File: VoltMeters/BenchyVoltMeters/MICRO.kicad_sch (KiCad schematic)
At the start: 18 parts, among them Y1 8MHz

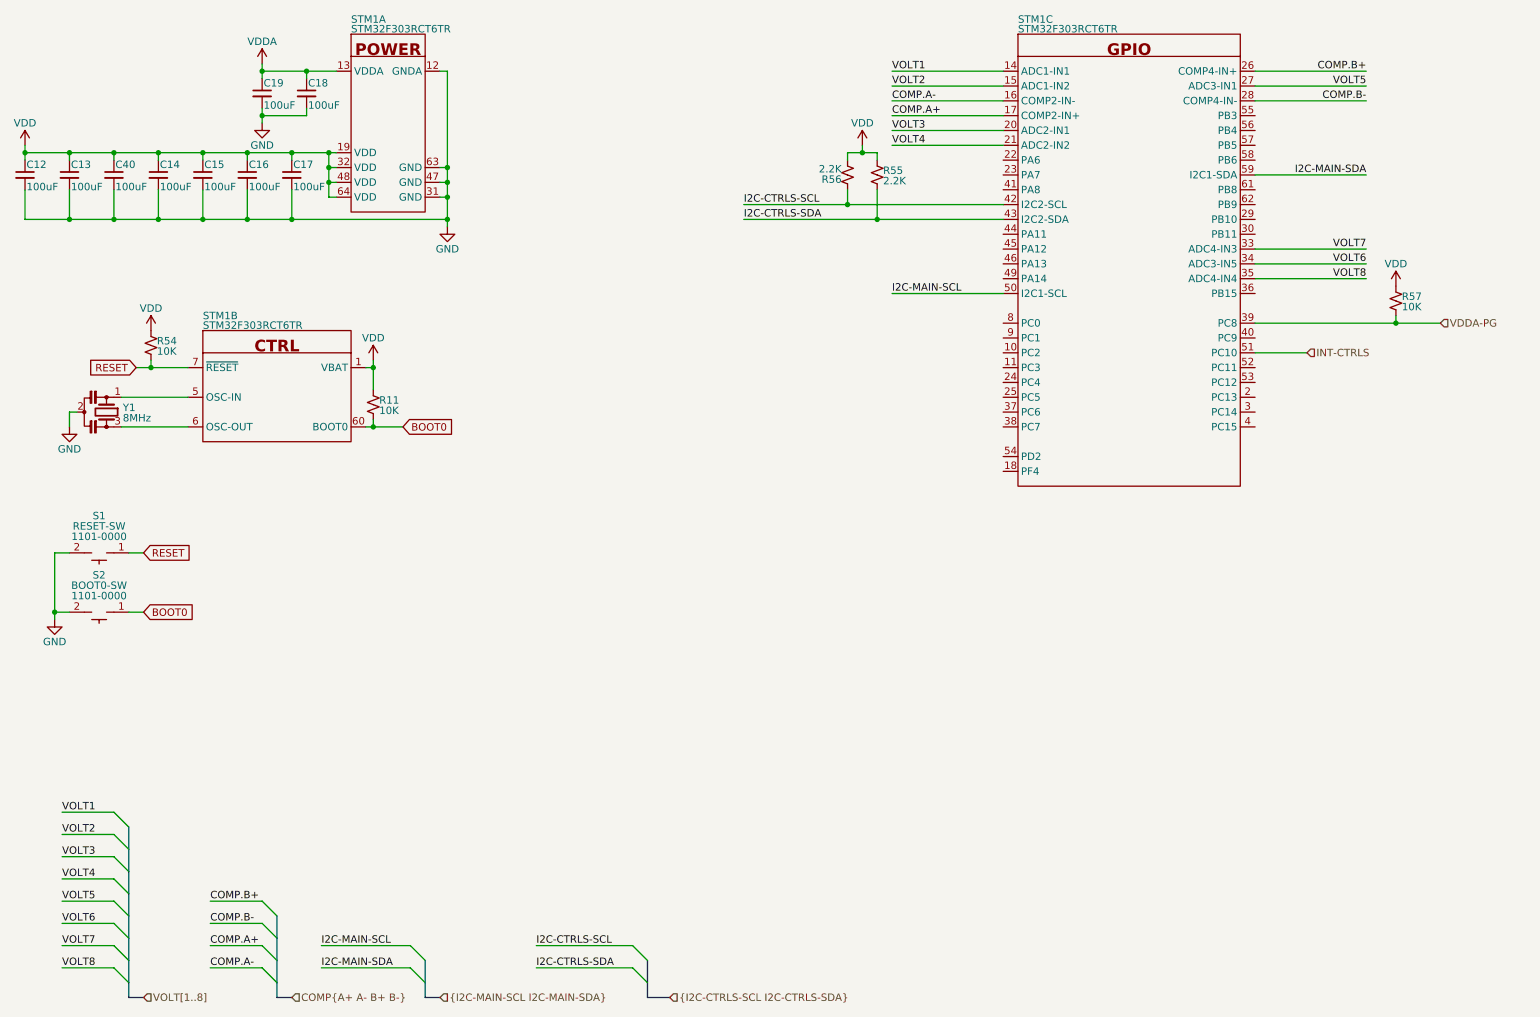
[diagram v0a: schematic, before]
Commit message: Add voltmeter PCB
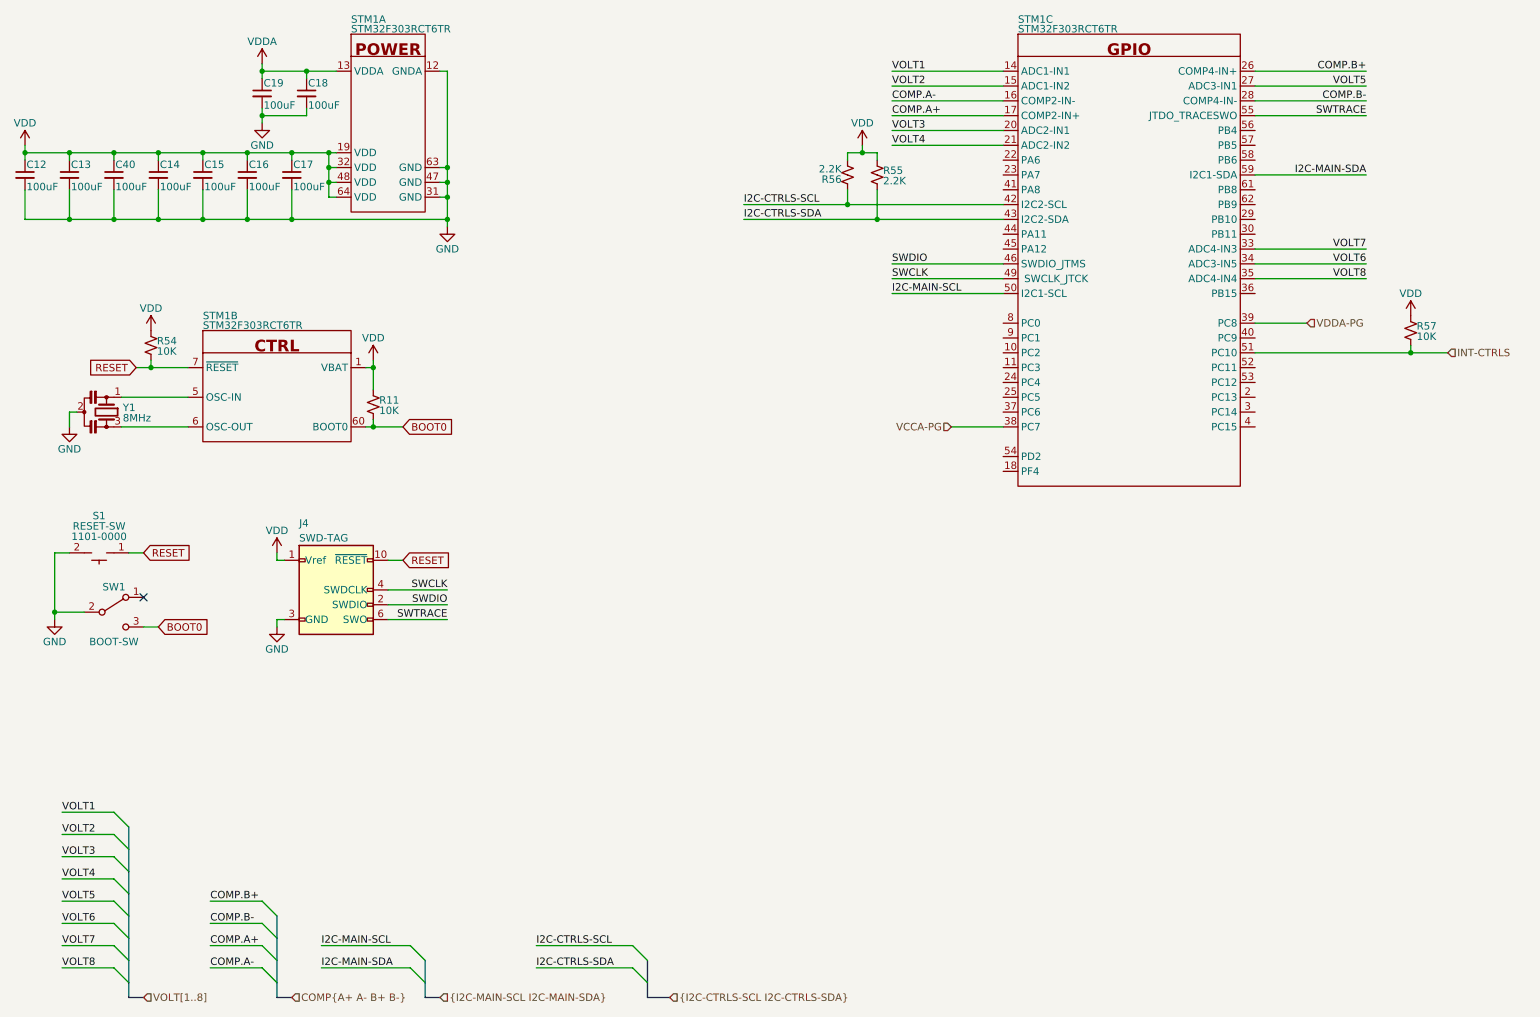
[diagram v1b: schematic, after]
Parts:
- removed S2: BOOT0-SW, Daxxn_Switches:TL3365AF180QG, symbol Daxxn_Buttons:GENERIC-SWITCH-2P
- added J4: SWD-TAG, Connector:Tag-Connect_TC2050-IDC-FP_2x05_P1.27mm_Vertical, symbol Daxxn_Connectors:SWD-TAG
- added SW1: BOOT-SW, Daxxn_Switches:EG1218, symbol Switch:SW_SPDT
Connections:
- net BOOT0: now also SW1.3 (C)
- net GND: now also J4.3 (GND), J4.5 (GND), J4.9 (GNDDetect), SW1.2 (B)
- net INT-CTRLS: now also R57.2
- net RESET: now also J4.10 (~{RESET})
- net VDD: now also J4.1 (Vref)
- net VDDA-PG: no longer R57.2
- net VCCA-PG: now reaches STM1.38 (PC7)
- net SWDIO: now reaches STM1.46 (PA13)
- net SWDIO: now also J4.2 (SWDIO)
- net SWCLK: now reaches STM1.49 (PA14)
- net SWCLK: now also J4.4 (SWDCLK)
- net SWTRACE: now reaches STM1.55 (PB3)
- net SWTRACE: now also J4.6 (SWO)
- no-connect marks 0 -> 1
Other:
- moved on the sheet: R57
